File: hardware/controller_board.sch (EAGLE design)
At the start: 122 parts, among them J1 FRSKY-GIMBAL-FRYSKY, J11 USB-MICROA-AMPHENOL-10118192-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, J2 FRSKY-GIMBAL-FRYSKY, J3 USB-MICROB-EDAC-690-005-299-0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, J4 AVR_SPI_PRG_6NS, J8 FRSKY-GIMBAL-2X-SERVO, J9 FRSKY-GIMBAL-2X-SERVO, P6 10K, U1 ATMEGA128RFA1, U2 DPDT-X2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

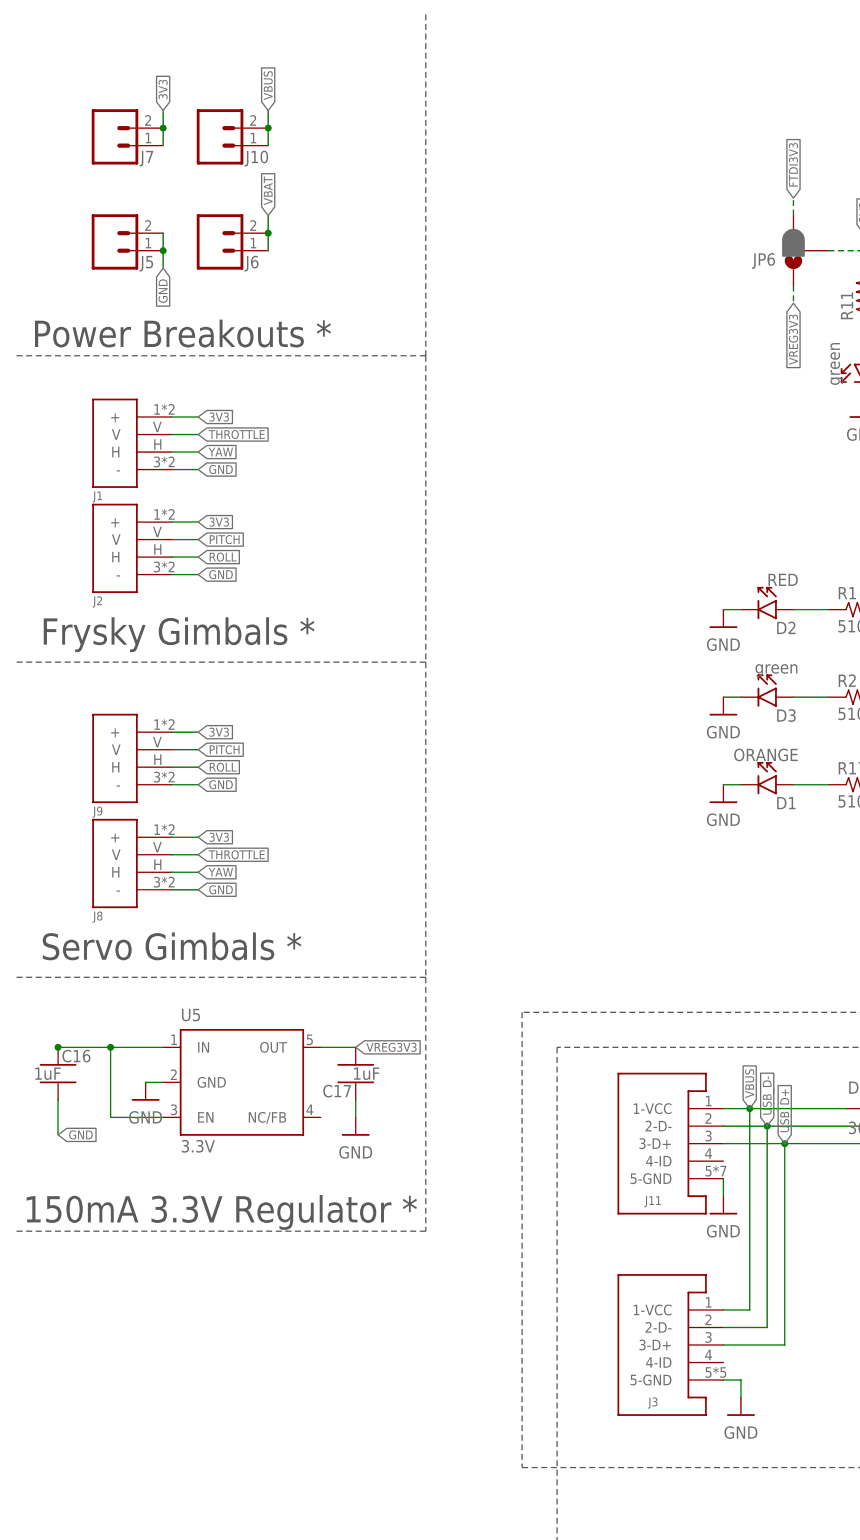
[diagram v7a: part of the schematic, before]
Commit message: new test points
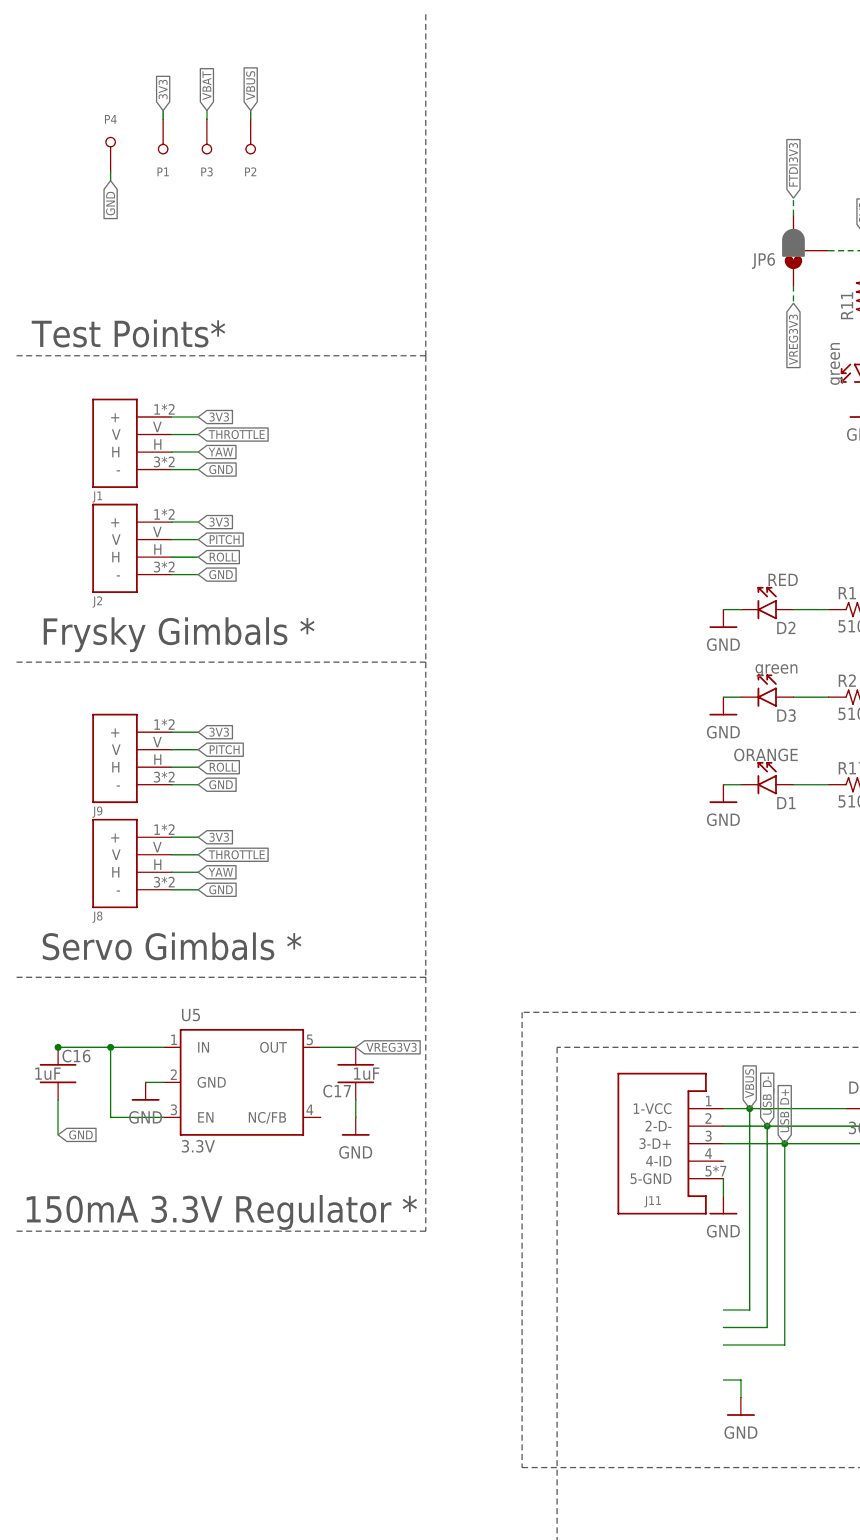
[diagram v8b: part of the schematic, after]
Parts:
- removed J10, J5, J6, J7: (no value), custom:MALE_HEADER_2POS-2X1-0.1IN
- removed J3: USB-MICROB-EDAC-690-005-299-043, RemoteParts:USB-MICROB-EDAC-690-005-299-043
- added P1, P2, P3, P4: TEST-POINT, RemoteParts:TEST-POINT
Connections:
- net 3V3: now also P1.T; no longer J7.1, J7.2
- net GND: now also P4.T; no longer J3.5-GND, J5.1, J5.2
- net USB_D+: no longer J3.3-D+
- net USB_D-: no longer J3.2-D-
- net VBAT: now also P3.T; no longer J6.1, J6.2
- net VBUS: now also P2.T; no longer J10.1, J10.2, J3.1-VCC
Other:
- note added: "Test Points*"
- note removed: "Power Breakouts *"
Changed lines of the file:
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@@
 <part name="GND21" library="quadparts_prebuilt" deviceset="GND" device=""/>
 <part name="U2" library="RemoteParts" deviceset="DPDT-X2" device="" package3d_urn="urn:adsk.eagle:package:3027343/1"/>
-<part name="J3" library="RemoteParts" deviceset="USB" device="-MICROB-EDAC-690-005-299-043"/>
 <part name="JP2" library="RemoteParts" deviceset="M06" device="-TH-RIGHT-ANGLE"/>
 <part name="GND1" library="quadparts_prebuilt" deviceset="GND" device=""/>
@@
 <attribute name="SPICEPREFIX" value="X"/>
 </part>
-<part name="J5" library="custom" deviceset="MALE_HEADER_2POS" device="-2X1-0.1IN">
-<attribute name="SPICEPREFIX" value="B"/>
-</part>
-<part name="J6" library="custom" deviceset="MALE_HEADER_2POS" device="-2X1-0.1IN">
-<attribute name="SPICEPREFIX" value="B"/>
-</part>
-<part name="J7" library="custom" deviceset="MALE_HEADER_2POS" device="-2X1-0.1IN">
-<attribute name="SPICEPREFIX" value="B"/>
-</part>
 <part name="P6" library="RemoteParts" deviceset="TRIMPOT" device="3386" value="10K">
 <attribute name="SPICEPREFIX" value="J"/>
@@
 <part name="R14" library="quadparts_prebuilt" deviceset="RESISTOR_" device="SMD-2012-0805-30K" value="30K"/>
 <part name="GND2" library="quadparts_prebuilt" deviceset="GND" device=""/>
-<part name="J10" library="custom" deviceset="MALE_HEADER_2POS" device="-2X1-0.1IN">
-<attribute name="SPICEPREFIX" value="B"/>
-</part>
 <part name="B3" library="RemoteParts" deviceset="HEADER-0.1IN-2POS" device="-SCREW">
 <attribute name="PIN1" value="+"/>
@@
 <part name="U5" library="quadparts_prebuilt" deviceset="TPS73633-DBVT" device="3V3" value="3.3V"/>
 <part name="JP6" library="RemoteParts" deviceset="JUMPER-SMT_3_1-NC_PASTE" device="_NO-SILK"/>
+<part name="P1" library="RemoteParts" deviceset="TEST-POINT" device=""/>
+<part name="P2" library="RemoteParts" deviceset="TEST-POINT" device=""/>
+<part name="P3" library="RemoteParts" deviceset="TEST-POINT" device=""/>
+<part name="P4" library="RemoteParts" deviceset="TEST-POINT" device=""/>
 </parts>
 <sheets>
@@
 <wire x1="63.5" y1="181.61" x2="63.5" y2="135.89" width="0.1524" layer="97" style="longdash"/>
 <wire x1="63.5" y1="135.89" x2="3.81" y2="135.89" width="0.1524" layer="97" style="longdash"/>
-<text x="6.35" y="227.33" size="3.81" layer="97">Power Breakouts *</text>
+<text x="6.35" y="227.33" size="3.81" layer="97">Test Points*</text>
 <text x="7.62" y="184.15" size="3.81" layer="97">Frysky Gimbals *</text>
 <text x="7.62" y="138.43" size="3.81" layer="97">Servo Gimbals *</text>
@@
 <instance part="GND21" gate="1" x="140.97" y="13.97"/>
 <instance part="U2" gate="G$1" x="276.86" y="96.52" rot="MR0"/>
-<instance part="J3" gate="A" x="101.6" y="82.55" rot="MR0"/>
 <instance part="JP2" gate="G$1" x="405.13" y="62.23" rot="MR0"/>
 <instance part="GND1" gate="1" x="281.94" y="76.2"/>
@@
 <instance part="F4" gate="G$1" x="353.06" y="29.21"/>
 <instance part="L1" gate="G$1" x="392.43" y="149.86"/>
-<instance part="J5" gate="G$1" x="15.24" y="238.76"/>
-<instance part="J6" gate="G$1" x="30.48" y="238.76"/>
-<instance part="J7" gate="G$1" x="15.24" y="254"/>
 <instance part="P6" gate="G$1" x="361.95" y="177.8"/>
 <instance part="R4" gate="G$1" x="359.41" y="144.78"/>
@@
 <instance part="R14" gate="G$1" x="222.25" y="22.86" rot="R90"/>
 <instance part="GND2" gate="1" x="222.25" y="15.24"/>
-<instance part="J10" gate="G$1" x="30.48" y="254"/>
 <instance part="B3" gate="G$1" x="242.57" y="34.29" rot="R180"/>
 <instance part="J11" gate="A" x="101.6" y="111.76" rot="MR0"/>
@@
 <instance part="U5" gate="G$1" x="27.94" y="113.03"/>
 <instance part="JP6" gate="G$1" x="116.84" y="241.3" rot="R180"/>
+<instance part="P1" gate="G$1" x="25.4" y="260.35" rot="R180"/>
+<instance part="P2" gate="G$1" x="38.1" y="260.35" rot="R180"/>
+<instance part="P3" gate="G$1" x="31.75" y="260.35" rot="R180"/>
+<instance part="P4" gate="G$1" x="17.78" y="252.73"/>
 </instances>
 <busses>
@@
 </segment>
 <segment>
-<pinref part="J3" gate="A" pin="5-GND"/>
 <wire x1="106.68" y1="77.47" x2="109.22" y2="77.47" width="0.1524" layer="91"/>
 <wire x1="109.22" y1="77.47" x2="109.22" y2="74.93" width="0.1524" layer="91"/>
@@
 </segment>
 <segment>
-<pinref part="J5" gate="G$1" pin="2"/>
-<pinref part="J5" gate="G$1" pin="1"/>
-<wire x1="25.4" y1="243.84" x2="25.4" y2="241.3" width="0.1524" layer="91"/>
-<wire x1="25.4" y1="241.3" x2="25.4" y2="238.76" width="0.1524" layer="91"/>
-<junction x="25.4" y="241.3"/>
-<label x="25.4" y="238.76" size="1.27" layer="95" rot="R270" xref="yes"/>
+<wire x1="17.78" y1="252.73" x2="17.78" y2="251.46" width="0.1524" layer="91"/>
+<label x="17.78" y="251.46" size="1.27" layer="95" rot="R270" xref="yes"/>
+<pinref part="P4" gate="G$1" pin="T"/>
 </segment>
 <segment>
@@
 </segment>
 <segment>
-<pinref part="J7" gate="G$1" pin="1"/>
-<pinref part="J7" gate="G$1" pin="2"/>
-<wire x1="25.4" y1="256.54" x2="25.4" y2="259.08" width="0.1524" layer="91"/>
-<wire x1="25.4" y1="261.62" x2="25.4" y2="259.08" width="0.1524" layer="91"/>
-<junction x="25.4" y="259.08"/>
+<wire x1="25.4" y1="261.62" x2="25.4" y2="260.35" width="0.1524" layer="91"/>
 <label x="25.4" y="261.62" size="1.27" layer="95" rot="R90" xref="yes"/>
+<pinref part="P1" gate="G$1" pin="T"/>
 </segment>
 <segment>
@@
 </segment>
 <segment>
-<pinref part="J6" gate="G$1" pin="1"/>
-<pinref part="J6" gate="G$1" pin="2"/>
-<wire x1="40.64" y1="241.3" x2="40.64" y2="243.84" width="0.1524" layer="91"/>
-<wire x1="40.64" y1="243.84" x2="40.64" y2="246.38" width="0.1524" layer="91"/>
-<junction x="40.64" y="243.84"/>
-<label x="40.64" y="246.38" size="1.27" layer="95" rot="R90" xref="yes"/>
+<wire x1="31.75" y1="260.35" x2="31.75" y2="261.62" width="0.1524" layer="91"/>
+<label x="31.75" y="261.62" size="1.27" layer="95" rot="R90" xref="yes"/>
+<pinref part="P3" gate="G$1" pin="T"/>
 </segment>
 <segment>
@@
 <net name="USB_D-" class="0">
 <segment>
-<pinref part="J3" gate="A" pin="2-D-"/>
 <wire x1="190.5" y1="114.3" x2="113.03" y2="114.3" width="0.1524" layer="91"/>
 <pinref part="U3" gate="G$1" pin="USBDM"/>
@@
 <net name="USB_D+" class="0">
 <segment>
-<pinref part="J3" gate="A" pin="3-D+"/>
 <wire x1="190.5" y1="111.76" x2="115.57" y2="111.76" width="0.1524" layer="91"/>
 <pinref part="U3" gate="G$1" pin="USBDP"/>
@@
 <wire x1="110.49" y1="116.84" x2="110.49" y2="87.63" width="0.1524" layer="91"/>
 <junction x="110.49" y="116.84"/>
-<pinref part="J3" gate="A" pin="1-VCC"/>
 <wire x1="106.68" y1="87.63" x2="110.49" y2="87.63" width="0.1524" layer="91"/>
 <pinref part="J11" gate="A" pin="1-VCC"/>
@@
 </segment>
 <segment>
-<pinref part="J10" gate="G$1" pin="1"/>
-<pinref part="J10" gate="G$1" pin="2"/>
-<wire x1="40.64" y1="256.54" x2="40.64" y2="259.08" width="0.1524" layer="91"/>
-<wire x1="40.64" y1="261.62" x2="40.64" y2="259.08" width="0.1524" layer="91"/>
-<junction x="40.64" y="259.08"/>
-<label x="40.64" y="261.62" size="1.27" layer="95" rot="R90" xref="yes"/>
-</segment>
-</net>
+<wire x1="38.1" y1="261.62" x2="38.1" y2="260.35" width="0.1524" layer="91"/>
+<label x="38.1" y="261.62" size="1.27" layer="95" rot="R90" xref="yes"/>
+<pinref part="P2" gate="G$1" pin="T"/>
+</segment>
+</net>
